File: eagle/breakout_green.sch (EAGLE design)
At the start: 19 parts, among them X1 734120110

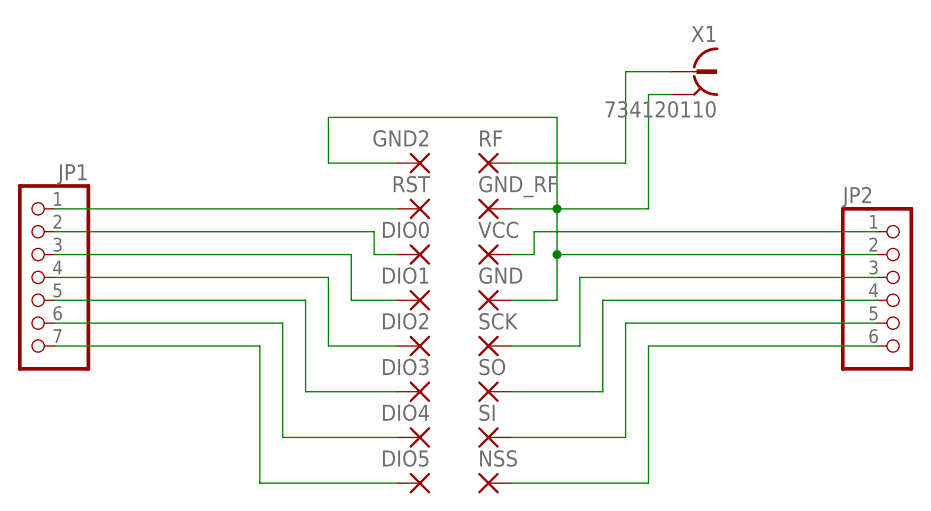
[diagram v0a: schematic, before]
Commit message: Shield and breakout layout update
Added a gap to the pin headers on LoRa breakout board and the shield to enforce breakout orientation.
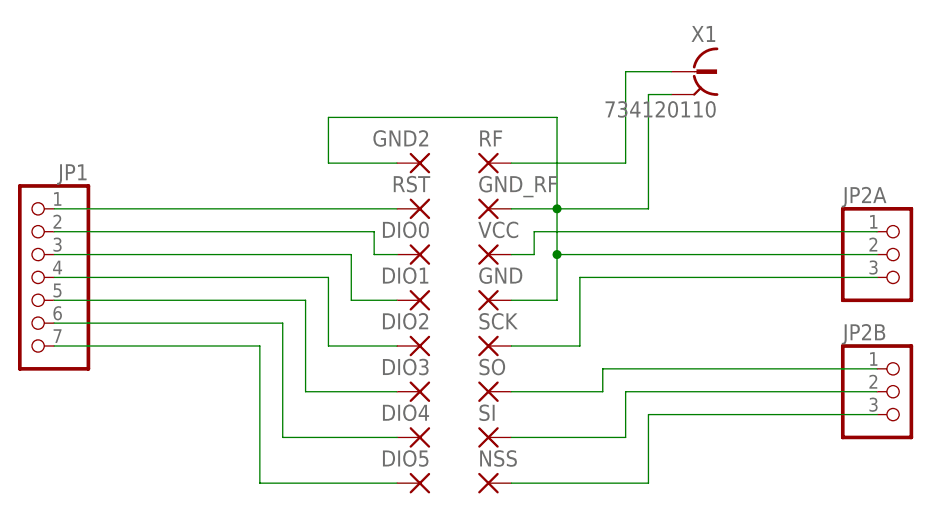
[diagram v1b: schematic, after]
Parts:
- removed JP2: (no value), pinhead:PINHD-1X6
- added JP2A, JP2B: (no value), pinhead:PINHD-1X3
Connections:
- net 3.3V: now also JP2A.1; no longer JP2.1
- net GND: now also JP2A.2; no longer JP2.2
- net MISO: now also JP2B.1; no longer JP2.4
- net MOSI: now also JP2B.2; no longer JP2.5
- net NSS: now also JP2B.3; no longer JP2.6
- net SCK: now also JP2A.3; no longer JP2.3
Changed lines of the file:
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@@
 <?xml version="1.0" encoding="utf-8"?>
 <!DOCTYPE eagle SYSTEM "eagle.dtd">
-<eagle version="7.5.0">
+<eagle version="8.0.2">
 <drawing>
 <settings>
@@
 <parts>
 <part name="JP1" library="pinhead" deviceset="PINHD-1X7" device=""/>
-<part name="JP2" library="pinhead" deviceset="PINHD-1X6" device=""/>
 <part name="RST" library="wirepad" deviceset="SMD2" device=""/>
 <part name="DIO0" library="wirepad" deviceset="SMD2" device=""/>
@@
 <part name="X1" library="con-coax" deviceset="734120110" device=""/>
 <part name="GND2" library="wirepad" deviceset="SMD2" device=""/>
+<part name="JP2A" library="pinhead" deviceset="PINHD-1X3" device=""/>
+<part name="JP2B" library="pinhead" deviceset="PINHD-1X3" device=""/>
 </parts>
 <sheets>
@@
 <instances>
 <instance part="JP1" gate="A" x="17.78" y="53.34" rot="MR0"/>
-<instance part="JP2" gate="A" x="114.3" y="50.8"/>
 <instance part="RST" gate="1" x="60.96" y="60.96" rot="MR0"/>
 <instance part="DIO0" gate="1" x="60.96" y="55.88" rot="MR0"/>
@@
 <instance part="X1" gate="G$1" x="91.44" y="76.2" rot="MR0"/>
 <instance part="GND2" gate="1" x="60.96" y="66.04" rot="MR0"/>
+<instance part="JP2A" gate="A" x="114.3" y="55.88"/>
+<instance part="JP2B" gate="A" x="114.3" y="40.64"/>
 </instances>
 <busses>
@@
 <segment>
 <pinref part="VCC" gate="1" pin="P"/>
-<pinref part="JP2" gate="A" pin="1"/>
 <wire x1="71.12" y1="55.88" x2="73.66" y2="55.88" width="0.1524" layer="91"/>
 <wire x1="73.66" y1="55.88" x2="73.66" y2="58.42" width="0.1524" layer="91"/>
 <wire x1="73.66" y1="58.42" x2="111.76" y2="58.42" width="0.1524" layer="91"/>
+<pinref part="JP2A" gate="A" pin="1"/>
 </segment>
 </net>
@@
 <wire x1="78.74" y1="45.72" x2="78.74" y2="53.34" width="0.1524" layer="91"/>
 <pinref part="SCK" gate="1" pin="P"/>
-<pinref part="JP2" gate="A" pin="3"/>
 <wire x1="78.74" y1="53.34" x2="111.76" y2="53.34" width="0.1524" layer="91"/>
+<pinref part="JP2A" gate="A" pin="3"/>
 </segment>
 </net>
@@
 <segment>
 <wire x1="71.12" y1="40.64" x2="81.28" y2="40.64" width="0.1524" layer="91"/>
-<wire x1="81.28" y1="40.64" x2="81.28" y2="50.8" width="0.1524" layer="91"/>
+<wire x1="81.28" y1="40.64" x2="81.28" y2="43.18" width="0.1524" layer="91"/>
 <pinref part="SO" gate="1" pin="P"/>
-<pinref part="JP2" gate="A" pin="4"/>
-<wire x1="81.28" y1="50.8" x2="111.76" y2="50.8" width="0.1524" layer="91"/>
+<wire x1="81.28" y1="43.18" x2="111.76" y2="43.18" width="0.1524" layer="91"/>
+<pinref part="JP2B" gate="A" pin="1"/>
 </segment>
 </net>
@@
 <segment>
 <wire x1="71.12" y1="35.56" x2="83.82" y2="35.56" width="0.1524" layer="91"/>
-<wire x1="83.82" y1="35.56" x2="83.82" y2="48.26" width="0.1524" layer="91"/>
+<wire x1="83.82" y1="35.56" x2="83.82" y2="40.64" width="0.1524" layer="91"/>
 <pinref part="SI" gate="1" pin="P"/>
-<pinref part="JP2" gate="A" pin="5"/>
-<wire x1="83.82" y1="48.26" x2="111.76" y2="48.26" width="0.1524" layer="91"/>
+<wire x1="83.82" y1="40.64" x2="111.76" y2="40.64" width="0.1524" layer="91"/>
+<pinref part="JP2B" gate="A" pin="2"/>
 </segment>
 </net>
@@
 <segment>
 <wire x1="71.12" y1="30.48" x2="86.36" y2="30.48" width="0.1524" layer="91"/>
-<wire x1="86.36" y1="30.48" x2="86.36" y2="45.72" width="0.1524" layer="91"/>
+<wire x1="86.36" y1="30.48" x2="86.36" y2="38.1" width="0.1524" layer="91"/>
 <pinref part="NSS" gate="1" pin="P"/>
-<pinref part="JP2" gate="A" pin="6"/>
-<wire x1="111.76" y1="45.72" x2="86.36" y2="45.72" width="0.1524" layer="91"/>
+<wire x1="111.76" y1="38.1" x2="86.36" y2="38.1" width="0.1524" layer="91"/>
+<pinref part="JP2B" gate="A" pin="3"/>
 </segment>
 </net>
@@
 <wire x1="76.2" y1="50.8" x2="76.2" y2="55.88" width="0.1524" layer="91"/>
 <pinref part="GND" gate="1" pin="P"/>
-<pinref part="JP2" gate="A" pin="2"/>
 <wire x1="76.2" y1="55.88" x2="111.76" y2="55.88" width="0.1524" layer="91"/>
 <pinref part="GND2" gate="1" pin="P"/>
@@
 <wire x1="86.36" y1="73.66" x2="88.9" y2="73.66" width="0.1524" layer="91"/>
 <junction x="76.2" y="60.96"/>
-</segment>
-</net>
+<pinref part="JP2A" gate="A" pin="2"/>
+</segment>
+</net>
